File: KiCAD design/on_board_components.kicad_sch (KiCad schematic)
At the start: 1 part

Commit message: finished conectors / sensors / converters
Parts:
- added C?: 0.1uF, symbol Device:C
- added C?: 1nF, symbol Device:C
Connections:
- net IP+: now reaches U?.1 (IP+), U?.2 (IP+)
- net IP-: now reaches U?.3 (IP-), U?.4 (IP-)
- net GND: now reaches U?.5 (GND)
- net GND: now also C?.1, C?.1
- net at U?.6 (FILTER): now also C?.2
- net CURRENT_MEASURE: now reaches U?.7 (VIOUT)
- net +7.2V: now reaches U?.8 (VCC)
- net +7.2V: now also C?.2
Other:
- note added: "CURRENT SENSOR"
- title: (none) -> Onboard Components
- moved on the sheet: U?
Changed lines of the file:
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@@
 (kicad_sch (version 20211123) (generator eeschema)
   (paper "A4")
-  (symbol (lib_id "Sensor_Current:ACS712xLCTR-20A") (at 55.7784 46.0248 0) (unit 1)
+  (title_block
+    (title "Onboard Components")
+  )
+  (junction (at 53.975 28.575) (diameter 0) (color 0 0 0 0)
+  )
+  (junction (at 53.975 74.295) (diameter 0) (color 0 0 0 0)
+  )
+  (wire (pts (xy 53.975 28.575) (xy 53.975 46.355))
+    (stroke (width 0) (type default) (color 0 0 0 0))
+  )
+  (wire (pts (xy 64.135 59.055) (xy 67.31 59.055))
+    (stroke (width 0) (type default) (color 0 0 0 0))
+  )
+  (wire (pts (xy 53.975 27.305) (xy 53.975 28.575))
+    (stroke (width 0) (type default) (color 0 0 0 0))
+  )
+  (wire (pts (xy 67.31 71.12) (xy 67.31 74.295))
+    (stroke (width 0) (type default) (color 0 0 0 0))
+  )
+  (wire (pts (xy 43.815 39.37) (xy 43.815 40.64))
+    (stroke (width 0) (type default) (color 0 0 0 0))
+  )
+  (polyline (pts (xy 112.395 13.97) (xy 112.395 85.09))
+    (stroke (width 0) (type default) (color 0 0 0 0))
+  )
+  (wire (pts (xy 43.815 31.75) (xy 43.815 28.575))
+    (stroke (width 0) (type default) (color 0 0 0 0))
+  )
+  (wire (pts (xy 67.31 59.055) (xy 67.31 63.5))
+    (stroke (width 0) (type default) (color 0 0 0 0))
+  )
+  (polyline (pts (xy 12.7 85.09) (xy 112.395 85.09))
+    (stroke (width 0) (type default) (color 0 0 0 0))
+  )
+  (wire (pts (xy 67.31 74.295) (xy 53.975 74.295))
+    (stroke (width 0) (type default) (color 0 0 0 0))
+  )
+  (wire (pts (xy 53.975 66.675) (xy 53.975 74.295))
+    (stroke (width 0) (type default) (color 0 0 0 0))
+  )
+  (wire (pts (xy 53.975 74.295) (xy 53.975 75.565))
+    (stroke (width 0) (type default) (color 0 0 0 0))
+  )
+  (wire (pts (xy 43.815 28.575) (xy 53.975 28.575))
+    (stroke (width 0) (type default) (color 0 0 0 0))
+  )
+  (text "CURRENT SENSOR\n" (at 15.24 22.86 0)
+    (effects (font (size 3.81 3.81)) (justify left bottom))
+  )
+  (hierarchical_label "IP+" (shape passive) (at 43.815 51.435 180)
+    (effects (font (size 1.27 1.27)) (justify right))
+  )
+  (hierarchical_label "IP-" (shape passive) (at 43.815 61.595 180)
+    (effects (font (size 1.27 1.27)) (justify right))
+  )
+  (hierarchical_label "CURRENT_MEASURE" (shape input) (at 64.135 56.515 0)
+    (effects (font (size 1.27 1.27)) (justify left))
+  )
+  (symbol (lib_id "power:GND") (at 43.815 40.64 0) (unit 1)
     (in_bom yes) (on_board yes) (fields_autoplaced)
-    (property "Reference" "U?" (id 0) (at 57.7978 33.02 0)
+    (property "Reference" "#PWR?" (id 0) (at 43.815 46.99 0)
+      (effects (font (size 1.27 1.27)) hide)
+    )
+    (property "Value" "GND" (id 1) (at 43.815 45.085 0))
+    (property "Footprint" "" (id 2) (at 43.815 40.64 0)
+      (effects (font (size 1.27 1.27)) hide)
+    )
+    (property "Datasheet" "" (id 3) (at 43.815 40.64 0)
+      (effects (font (size 1.27 1.27)) hide)
+    )
+    (pin "1")
+  )
+  (symbol (lib_id "Device:C") (at 43.815 35.56 0) (mirror x) (unit 1)
+    (in_bom yes) (on_board yes) (fields_autoplaced)
+    (property "Reference" "C?" (id 0) (at 40.005 34.2899 0)
+      (effects (font (size 1.27 1.27)) (justify right))
+    )
+    (property "Value" "0.1uF" (id 1) (at 40.005 36.8299 0)
+      (effects (font (size 1.27 1.27)) (justify right))
+    )
+    (property "Footprint" "" (id 2) (at 44.7802 31.75 0)
+      (effects (font (size 1.27 1.27)) hide)
+    )
+    (property "Datasheet" "~" (id 3) (at 43.815 35.56 0)
+      (effects (font (size 1.27 1.27)) hide)
+    )
+    (pin "1")
+    (pin "2")
+  )
+  (symbol (lib_id "composants_projet:+7.2V") (at 53.975 27.305 0) (unit 1)
+    (in_bom yes) (on_board yes) (fields_autoplaced)
+    (property "Reference" "#PWR?" (id 0) (at 53.975 31.115 0)
+      (effects (font (size 1.27 1.27)) hide)
+    )
+    (property "Value" "+12V" (id 1) (at 55.88 26.0349 0)
       (effects (font (size 1.27 1.27)) (justify left))
     )
-    (property "Value" "ACS712xLCTR-20A" (id 1) (at 57.7978 35.56 0)
+    (property "Footprint" "" (id 2) (at 53.975 27.305 0)
+      (effects (font (size 1.27 1.27)) hide)
+    )
+    (property "Datasheet" "" (id 3) (at 53.975 27.305 0)
+      (effects (font (size 1.27 1.27)) hide)
+    )
+    (pin "1")
+  )
+  (symbol (lib_id "Device:C") (at 67.31 67.31 180) (unit 1)
+    (in_bom yes) (on_board yes) (fields_autoplaced)
+    (property "Reference" "C?" (id 0) (at 71.12 66.0399 0)
+      (effects (font (size 1.27 1.27)) (justify right))
+    )
+    (property "Value" "1nF" (id 1) (at 71.12 68.5799 0)
+      (effects (font (size 1.27 1.27)) (justify right))
+    )
+    (property "Footprint" "" (id 2) (at 66.3448 63.5 0)
+      (effects (font (size 1.27 1.27)) hide)
+    )
+    (property "Datasheet" "~" (id 3) (at 67.31 67.31 0)
+      (effects (font (size 1.27 1.27)) hide)
+    )
+    (pin "1")
+    (pin "2")
+  )
+  (symbol (lib_id "power:GND") (at 53.975 75.565 0) (unit 1)
+    (in_bom yes) (on_board yes) (fields_autoplaced)
+    (property "Reference" "#PWR?" (id 0) (at 53.975 81.915 0)
+      (effects (font (size 1.27 1.27)) hide)
+    )
+    (property "Value" "GND" (id 1) (at 53.975 80.01 0))
+    (property "Footprint" "" (id 2) (at 53.975 75.565 0)
+      (effects (font (size 1.27 1.27)) hide)
+    )
+    (property "Datasheet" "" (id 3) (at 53.975 75.565 0)
+      (effects (font (size 1.27 1.27)) hide)
+    )
+    (pin "1")
+  )
+  (symbol (lib_id "Sensor_Current:ACS712xLCTR-20A") (at 53.975 56.515 0) (unit 1)
+    (in_bom yes) (on_board yes)
+    (property "Reference" "U?" (id 0) (at 55.9944 43.5102 0)
       (effects (font (size 1.27 1.27)) (justify left))
     )
-    (property "Footprint" "Package_SO:SOIC-8_3.9x4.9mm_P1.27mm" (id 2) (at 58.3184 54.9148 0)
+    (property "Value" "ACS712xLCTR-20A" (id 1) (at 55.9944 46.0502 0)
+      (effects (font (size 1.27 1.27)) (justify left))
+    )
+    (property "Footprint" "Package_SO:SOIC-8_3.9x4.9mm_P1.27mm" (id 2) (at 56.515 65.405 0)
       (effects (font (size 1.27 1.27) italic) (justify left) hide)
     )
-    (property "Datasheet" "http://www.allegromicro.com/~/media/Files/Datasheets/ACS712-Datasheet.ashx?la=en" (id 3) (at 55.7784 46.0248 0)
+    (property "Datasheet" "http://www.allegromicro.com/~/media/Files/Datasheets/ACS712-Datasheet.ashx?la=en" (id 3) (at 53.975 56.515 0)
       (effects (font (size 1.27 1.27)) hide)
     )

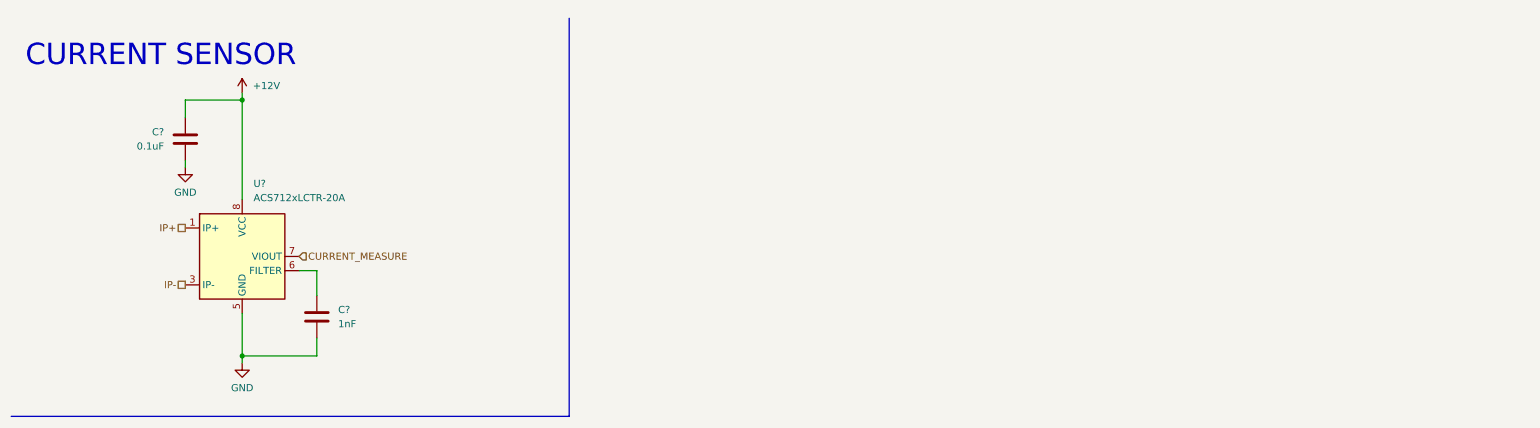
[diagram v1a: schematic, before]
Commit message: labeling and add of components. STM32 pin selected
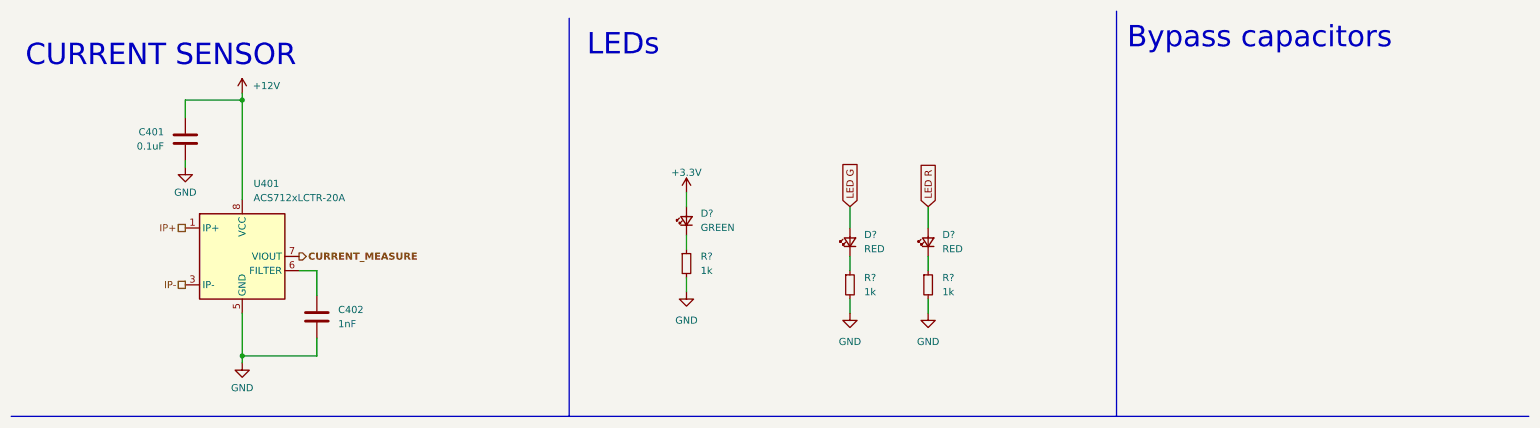
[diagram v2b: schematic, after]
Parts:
- added D?: GREEN, LED_SMD:LED_0603_1608Metric_Pad1.05x0.95mm_HandSolder, symbol Device:LED_Small
- added D? (x2): RED, LED_SMD:LED_0603_1608Metric_Pad1.05x0.95mm_HandSolder, symbol Device:LED_Small
- added R? (x3): 1k, Resistor_SMD:R_0603_1608Metric_Pad0.98x0.95mm_HandSolder, symbol Device:R_Small
- gave numbers to parts that had none: 3
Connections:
- net GND: now also R?.2, R?.2, R?.2
- new net: D?.1 (K), R?.1 (x3)
- new net +3V3: D?.2 (A)
- new net LED G: D?.2 (A)
- new net LED R: D?.2 (A)
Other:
- note added: "Bypass capacitors"
- note added: "LEDs"

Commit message: correction of errors
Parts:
- gave numbers to parts that had none: 6
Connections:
- net IP- is gone; now on net +12V: U401.3 (IP-), U401.4 (IP-)
- net +3V3 renamed +3.3V
- net +7.2V renamed +12V
- net LED G renamed LED1
- net LED R renamed LED2
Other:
- moved on the sheet: D402
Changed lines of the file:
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@@
     (stroke (width 0) (type default) (color 0 0 0 0))
   )
-  (wire (pts (xy 162.56 47.625) (xy 162.56 51.435))
-    (stroke (width 0) (type default) (color 0 0 0 0))
-  )
-  (wire (pts (xy 162.56 56.515) (xy 162.56 59.055))
+  (wire (pts (xy 40.64 61.595) (xy 43.815 61.595))
+    (stroke (width 0) (type default) (color 0 0 0 0))
+  )
+  (wire (pts (xy 162.56 47.625) (xy 162.56 52.07))
+    (stroke (width 0) (type default) (color 0 0 0 0))
+  )
+  (wire (pts (xy 162.56 57.15) (xy 162.56 59.055))
     (stroke (width 0) (type default) (color 0 0 0 0))
   )
   (wire (pts (xy 162.56 64.135) (xy 162.56 66.675))
+    (stroke (width 0) (type default) (color 0 0 0 0))
+  )
+  (wire (pts (xy 40.64 59.055) (xy 40.64 61.595))
     (stroke (width 0) (type default) (color 0 0 0 0))
   )
@@
     (effects (font (size 3.81 3.81)) (justify left bottom))
   )
-  (global_label "LED G" (shape input) (at 162.56 47.625 90) (fields_autoplaced)
-    (effects (font (size 1.27 1.27)) (justify left))
-    (property "Intersheet References" "${INTERSHEET_REFS}" (id 0) (at 162.4806 39.5271 90)
-      (effects (font (size 1.27 1.27)) (justify left) hide)
-    )
-  )
-  (global_label "LED R" (shape input) (at 176.53 47.625 90) (fields_autoplaced)
-    (effects (font (size 1.27 1.27)) (justify left))
-    (property "Intersheet References" "${INTERSHEET_REFS}" (id 0) (at 176.4506 39.5271 90)
-      (effects (font (size 1.27 1.27)) (justify left) hide)
-    )
-  )
   (hierarchical_label "IP+" (shape passive) (at 43.815 51.435 180)
     (effects (font (size 1.27 1.27)) (justify right))
   )
-  (hierarchical_label "IP-" (shape passive) (at 43.815 61.595 180)
-    (effects (font (size 1.27 1.27)) (justify right))
-  )
   (hierarchical_label "CURRENT_MEASURE" (shape output) (at 64.135 56.515 0)
     (effects (font (size 1.27 1.27) (thickness 0.254) bold) (justify left))
   )
+  (hierarchical_label "LED2" (shape input) (at 176.53 47.625 90)
+    (effects (font (size 1.27 1.27)) (justify left))
+  )
+  (hierarchical_label "LED1" (shape input) (at 162.56 47.625 90)
+    (effects (font (size 1.27 1.27) bold) (justify left))
+  )
   (symbol (lib_id "power:GND") (at 43.815 40.64 0) (unit 1)
     (in_bom yes) (on_board yes) (fields_autoplaced)
@@
     (pin "2")
   )
-  (symbol (lib_id "composants_projet:+7.2V") (at 53.975 27.305 0) (unit 1)
-    (in_bom yes) (on_board yes) (fields_autoplaced)
-    (property "Reference" "#PWR0402" (id 0) (at 53.975 31.115 0)
-      (effects (font (size 1.27 1.27)) hide)
-    )
-    (property "Value" "+12V" (id 1) (at 55.88 26.0349 0)
-      (effects (font (size 1.27 1.27)) (justify left))
-    )
+  (symbol (lib_id "power:+12V") (at 53.975 27.305 0) (unit 1)
+    (in_bom yes) (on_board yes) (fields_autoplaced)
+    (property "Reference" "#PWR0111" (id 0) (at 53.975 31.115 0)
+      (effects (font (size 1.27 1.27)) hide)
+    )
+    (property "Value" "+12V" (id 1) (at 53.975 22.225 0))
     (property "Footprint" "" (id 2) (at 53.975 27.305 0)
       (effects (font (size 1.27 1.27)) hide)
     )
     (property "Datasheet" "" (id 3) (at 53.975 27.305 0)
-      (effects (font (size 1.27 1.27)) hide)
-    )
-    (pin "1")
-  )
-  (symbol (lib_id "power:+3.3V") (at 133.35 45.085 0) (unit 1)
-    (in_bom yes) (on_board yes) (fields_autoplaced)
-    (property "Reference" "#PWR?" (id 0) (at 133.35 48.895 0)
-      (effects (font (size 1.27 1.27)) hide)
-    )
-    (property "Value" "+3.3V" (id 1) (at 133.35 41.529 0))
-    (property "Footprint" "" (id 2) (at 133.35 45.085 0)
-      (effects (font (size 1.27 1.27)) hide)
-    )
-    (property "Datasheet" "" (id 3) (at 133.35 45.085 0)
       (effects (font (size 1.27 1.27)) hide)
     )
@@
   (symbol (lib_id "Device:R_Small") (at 176.53 61.595 0) (unit 1)
     (in_bom yes) (on_board yes) (fields_autoplaced)
-    (property "Reference" "R?" (id 0) (at 179.07 60.3249 0)
+    (property "Reference" "R403" (id 0) (at 179.07 60.3249 0)
       (effects (font (size 1.27 1.27)) (justify left))
     )
@@
   (symbol (lib_id "power:GND") (at 133.35 62.865 0) (unit 1)
     (in_bom yes) (on_board yes) (fields_autoplaced)
-    (property "Reference" "#PWR?" (id 0) (at 133.35 69.215 0)
+    (property "Reference" "#PWR0108" (id 0) (at 133.35 69.215 0)
       (effects (font (size 1.27 1.27)) hide)
     )
@@
   (symbol (lib_id "Device:LED_Small") (at 133.35 50.165 90) (unit 1)
     (in_bom yes) (on_board yes) (fields_autoplaced)
-    (property "Reference" "D?" (id 0) (at 135.89 48.8314 90)
+    (property "Reference" "D401" (id 0) (at 135.89 48.8314 90)
       (effects (font (size 1.27 1.27)) (justify right))
     )
@@
   (symbol (lib_id "power:GND") (at 176.53 66.675 0) (unit 1)
     (in_bom yes) (on_board yes) (fields_autoplaced)
-    (property "Reference" "#PWR?" (id 0) (at 176.53 73.025 0)
+    (property "Reference" "#PWR0106" (id 0) (at 176.53 73.025 0)
       (effects (font (size 1.27 1.27)) hide)
     )
@@
     (pin "8")
   )
-  (symbol (lib_id "Device:LED_Small") (at 162.56 53.975 90) (unit 1)
-    (in_bom yes) (on_board yes) (fields_autoplaced)
-    (property "Reference" "D?" (id 0) (at 165.1 52.6414 90)
-      (effects (font (size 1.27 1.27)) (justify right))
-    )
-    (property "Value" "RED" (id 1) (at 165.1 55.1814 90)
-      (effects (font (size 1.27 1.27)) (justify right))
-    )
-    (property "Footprint" "LED_SMD:LED_0603_1608Metric_Pad1.05x0.95mm_HandSolder" (id 2) (at 162.56 53.975 90)
-      (effects (font (size 1.27 1.27)) hide)
-    )
-    (property "Datasheet" "~" (id 3) (at 162.56 53.975 90)
-      (effects (font (size 1.27 1.27)) hide)
-    )
-    (pin "1")
-    (pin "2")
+  (symbol (lib_id "Device:LED_Small") (at 162.56 54.61 90) (unit 1)
+    (in_bom yes) (on_board yes) (fields_autoplaced)
+    (property "Reference" "D402" (id 0) (at 165.1 53.2764 90)
+      (effects (font (size 1.27 1.27)) (justify right))
+    )
+    (property "Value" "RED" (id 1) (at 165.1 55.8164 90)
+      (effects (font (size 1.27 1.27)) (justify right))
+    )
+    (property "Footprint" "LED_SMD:LED_0603_1608Metric_Pad1.05x0.95mm_HandSolder" (id 2) (at 162.56 54.61 90)
+      (effects (font (size 1.27 1.27)) hide)
+    )
+    (property "Datasheet" "~" (id 3) (at 162.56 54.61 90)
+      (effects (font (size 1.27 1.27)) hide)
+    )
+    (pin "1")
+    (pin "2")
+  )
+  (symbol (lib_id "power:+3.3V") (at 133.35 45.085 0) (unit 1)
+    (in_bom yes) (on_board yes) (fields_autoplaced)
+    (property "Reference" "#PWR0109" (id 0) (at 133.35 48.895 0)
+      (effects (font (size 1.27 1.27)) hide)
+    )
+    (property "Value" "+3.3V" (id 1) (at 133.35 39.37 0))
+    (property "Footprint" "" (id 2) (at 133.35 45.085 0)
+      (effects (font (size 1.27 1.27)) hide)
+    )
+    (property "Datasheet" "" (id 3) (at 133.35 45.085 0)
+      (effects (font (size 1.27 1.27)) hide)
+    )
+    (pin "1")
   )
   (symbol (lib_id "Device:R_Small") (at 162.56 61.595 0) (unit 1)
     (in_bom yes) (on_board yes) (fields_autoplaced)
-    (property "Reference" "R?" (id 0) (at 165.1 60.3249 0)
+    (property "Reference" "R402" (id 0) (at 165.1 60.3249 0)
       (effects (font (size 1.27 1.27)) (justify left))
     )
@@
   (symbol (lib_id "Device:R_Small") (at 133.35 57.785 0) (unit 1)
     (in_bom yes) (on_board yes) (fields_autoplaced)
-    (property "Reference" "R?" (id 0) (at 135.89 56.5149 0)
+    (property "Reference" "R401" (id 0) (at 135.89 56.5149 0)
       (effects (font (size 1.27 1.27)) (justify left))
     )
@@
   (symbol (lib_id "Device:LED_Small") (at 176.53 53.975 90) (unit 1)
     (in_bom yes) (on_board yes) (fields_autoplaced)
-    (property "Reference" "D?" (id 0) (at 179.07 52.6414 90)
+    (property "Reference" "D403" (id 0) (at 179.07 52.6414 90)
       (effects (font (size 1.27 1.27)) (justify right))
     )
@@
   (symbol (lib_id "power:GND") (at 162.56 66.675 0) (unit 1)
     (in_bom yes) (on_board yes) (fields_autoplaced)
-    (property "Reference" "#PWR?" (id 0) (at 162.56 73.025 0)
+    (property "Reference" "#PWR0107" (id 0) (at 162.56 73.025 0)
       (effects (font (size 1.27 1.27)) hide)
     )
@@
       (effects (font (size 1.27 1.27)) hide)
     )
+    (pin "1")
+  )
+  (symbol (lib_id "power:+12V") (at 40.64 59.055 0) (unit 1)
+    (in_bom yes) (on_board yes)
+    (property "Reference" "#PWR0103" (id 0) (at 40.64 62.865 0)
+      (effects (font (size 1.27 1.27)) hide)
+    )
+    (property "Value" "+12V" (id 1) (at 40.64 55.245 0))
+    (property "Footprint" "" (id 2) (at 40.64 59.055 0)
+      (effects (font (size 1.27 1.27)) hide)
+    )
+    (property "Datasheet" "" (id 3) (at 40.64 59.055 0)
+      (effects (font (size 1.27 1.27)) hide)
+    )

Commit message: add of footprint and nucleo as a reference
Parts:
- C401, C402: footprint (none) -> Capacitor_SMD:C_0603_1608Metric_Pad1.08x0.95mm_HandSolder
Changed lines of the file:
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@@
       (effects (font (size 1.27 1.27)) (justify right))
     )
-    (property "Footprint" "" (id 2) (at 44.7802 31.75 0)
+    (property "Footprint" "Capacitor_SMD:C_0603_1608Metric_Pad1.08x0.95mm_HandSolder" (id 2) (at 44.7802 31.75 0)
       (effects (font (size 1.27 1.27)) hide)
     )
@@
       (effects (font (size 1.27 1.27)) (justify right))
     )
-    (property "Footprint" "" (id 2) (at 66.3448 63.5 0)
+    (property "Footprint" "Capacitor_SMD:C_0603_1608Metric_Pad1.08x0.95mm_HandSolder" (id 2) (at 66.3448 63.5 0)
       (effects (font (size 1.27 1.27)) hide)
     )
